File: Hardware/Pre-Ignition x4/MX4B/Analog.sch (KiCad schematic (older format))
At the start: 55 parts, among them J4 VR_Header, U3 SRV05-4-P-T7, U4 SRV05-4-P-T7, U5 SRV05-4-P-T7, U6 SRV05-4-P-T7

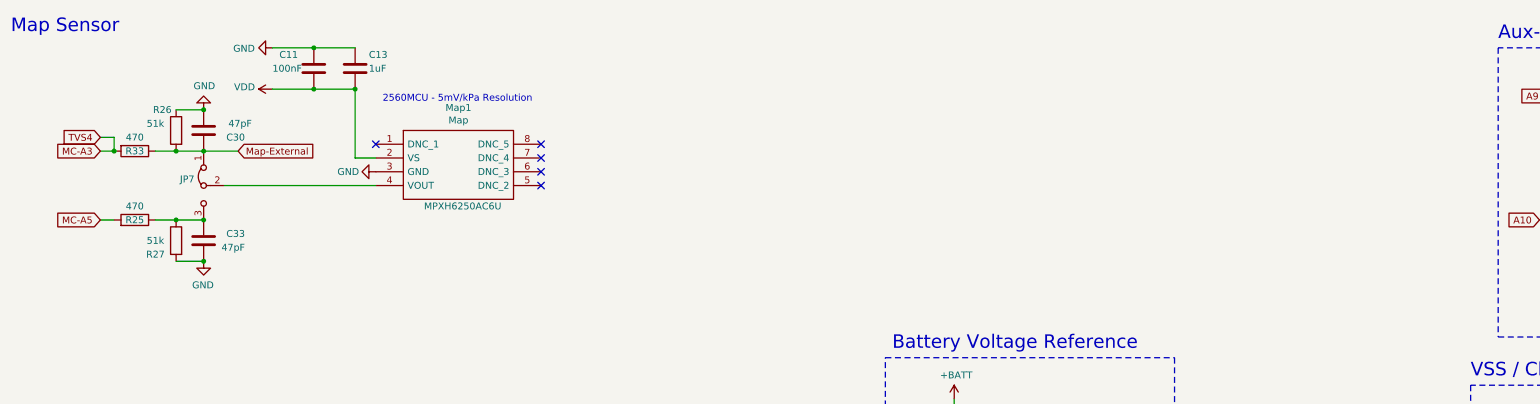
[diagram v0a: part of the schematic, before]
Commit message: Pre-Ignition x2 Initial Upload, MX4B Production.
Pre-Ignition x2 Initial Upload - 2 Channel Speeduino compatible ECU
Pre-Ignition x4 MX4B (revision B) - minor updates, BOM changes, connectors moved to bottom side of board.
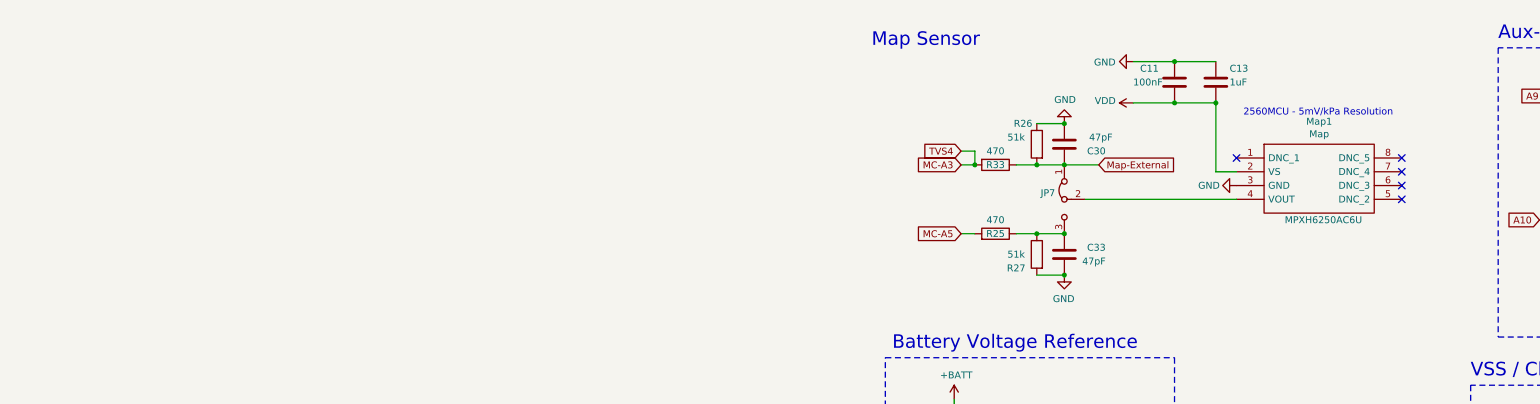
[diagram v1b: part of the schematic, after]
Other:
- moved on the sheet: C11, C13, C30, C33, JP7, Map1, R25, R26, R27, R33

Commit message: bom fix
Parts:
- R34, R61: value 470 -> 220; JLC C23179 -> (none); LCSC C23179 -> C22962
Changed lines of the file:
@@
 P 3150 6950
 F 0 "R61" V 2943 6950 50  0000 C CNN
-F 1 "470" V 3034 6950 50  0000 C CNN
+F 1 "220" V 3034 6950 50  0000 C CNN
 F 2 "Resistor_SMD:R_0603_1608Metric" V 3080 6950 50  0001 C CNN
 F 3 "~" H 3150 6950 50  0001 C CNN
-F 4 "C23179" H 3150 6950 50  0001 C CNN "JLC"
-F 5 "C23179" H 3150 6950 50  0001 C CNN "LCSC"
+F 4 "C22962" H 3150 6950 50  0001 C CNN "LCSC"
 	1    3150 6950
 	0    1    1    0
@@
 P 3150 5850
 F 0 "R34" V 2943 5850 50  0000 C CNN
-F 1 "470" V 3034 5850 50  0000 C CNN
+F 1 "220" V 3034 5850 50  0000 C CNN
 F 2 "Resistor_SMD:R_0603_1608Metric" V 3080 5850 50  0001 C CNN
 F 3 "~" H 3150 5850 50  0001 C CNN
-F 4 "C23179" H 3150 5850 50  0001 C CNN "JLC"
-F 5 "C23179" H 3150 5850 50  0001 C CNN "LCSC"
+F 4 "C22962" H 3150 5850 50  0001 C CNN "LCSC"
 	1    3150 5850
 	0    1    1    0
